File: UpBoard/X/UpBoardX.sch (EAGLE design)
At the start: 120 parts, among them CN1 100nF, CN2 100nF, CN3 100nF, CN4 100nF, IC1 SAM3X8E(ARDUINO), IC2 MEGA16U2-MU, J1 2POSTERMINALBLOCK.25"PITCH, Q1 FDS5680, Q2 FDS5680, Q3 FDS5680, Q4 FDS5680, Q5 SSMJ328R,LF, Q6 2N7002E, Q8 2N7002E, X1 COMS, X2 COMS, X3 GP, X4 CTRL/PYRO, Y1 FH1200001, Y2 ABS05, Y3 406C35D16M00000

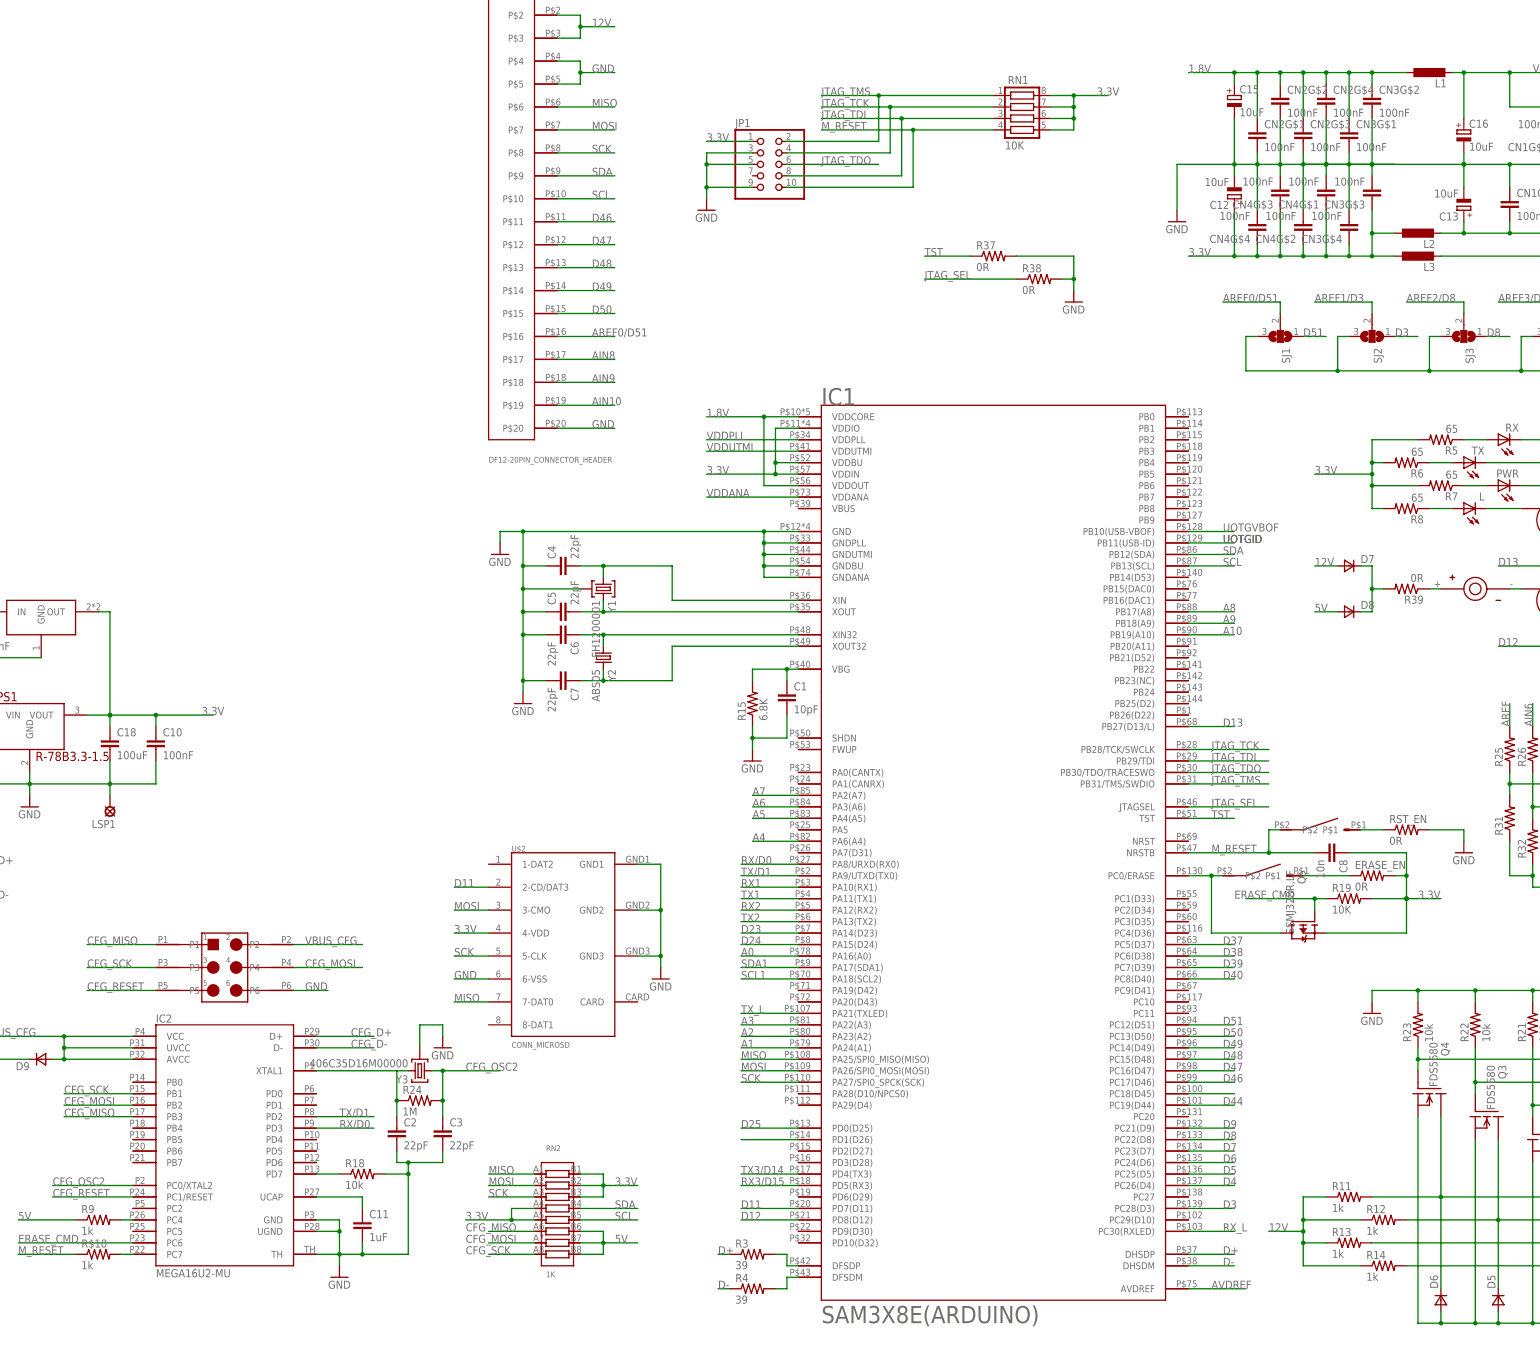
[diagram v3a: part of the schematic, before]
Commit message: Finished labeling, removed SPI pull ups
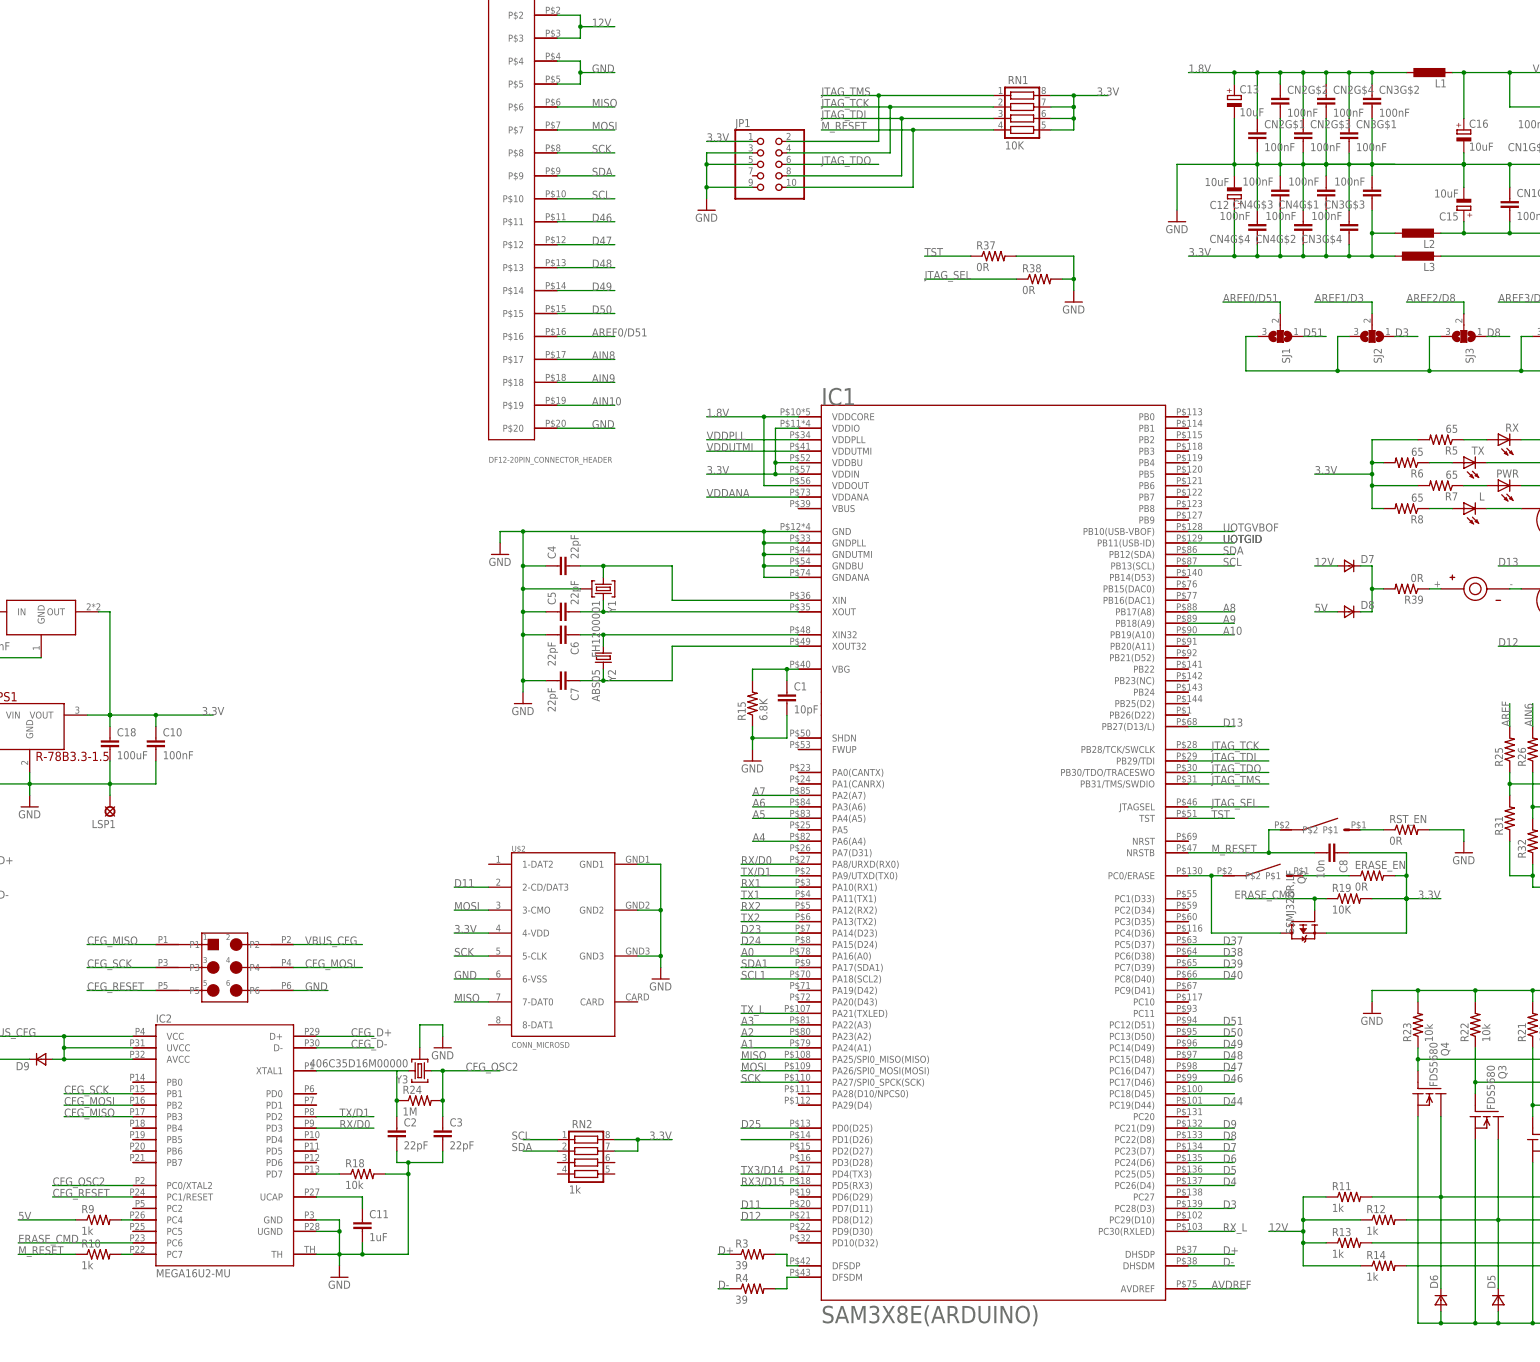
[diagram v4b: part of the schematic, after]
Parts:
- RN2: value 1K -> 1k; device resistor-net:EXB-2HV102JV -> resistor-net:CTS742C083
- renumbered R$10 to R10
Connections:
- net 1.8V: now also C13.+; no longer C15.+
- net 3.3V: now also RN2.7, RN2.8; no longer RN2.A4, RN2.A5, RN2.B1, RN2.B2, RN2.B3
- net 5V: no longer RN2.B6, RN2.B7, RN2.B8
- net CFG_MISO: no longer RN2.A6
- net CFG_MOSI: no longer RN2.A7
- net CFG_SCK: no longer RN2.A8
- net MISO: no longer RN2.A1
- net MOSI: no longer RN2.A2
- net SCK: no longer RN2.A3
- net SCL: now also RN2.1; no longer RN2.B5
- net SDA: now also RN2.2; no longer RN2.B4
- net VDDANA: now also C15.+; no longer C13.+
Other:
- moved on the sheet: C13, C15

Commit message: First fixes, schematic appearance changes
Connected D+ line on native USB port. Added title block and reorganized
schematic to fit on a size C sheet. Revision number is now 1.
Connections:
- net D+: now also US1.D+
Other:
- note added: "1"
- note added: "Assy:"
- note added: "C"
- note added: "C:/Users/Patrick Chizek/Pictures/CPSSLOGO.bmp"
- note added: "Cal Poly Space Systems"
- note added: "Date:"
- note added: "File: UpBoardX.sch"
- note added: "Project Title:"
- note added: "Revision:"
- note added: "Sheet 1 of 2"
- note added: "Sheet Title:"
- note added: "Size:"
- note added: "UBX Full Schematic"
- note added: "UpBoard X"
- note removed: "SENSOR PACKAGE"
- note removed: "UPBOARD X"
- moved on the sheet: C1, C10, C11, C12, C13, C14, C15, C16, C17, C18, C2, C3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

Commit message: Organized power supply into own module
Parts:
- removed C10, C9: 100nF, resistor:C-EUC0603
- removed C17, C18: 100uF, resistor:C-EUC0805
- removed D1: S10M-TP, UpBoard:S10M-TP
- removed D2: (no value), zetex:DSOD323
- removed PS1: R-78B3.3-1.5, UpBoard B:R-78B3.3-1.5
- removed PS2: AZ1117C, UpBoard B:AZ1117C
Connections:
- removed net VIN: D1.+, J1.P$1
- net 12V: no longer D1.-, D2.A
- net 3.3V: no longer C10.1, C18.1, PS1.VOUT, PS2.OUT
- net 5V: no longer C17.1, C9.1, PS2.IN
- net GND: no longer C10.2, C17.2, C18.2, C9.2, PS1.GND, PS2.GND
- net N$7: now also J1.P$1; no longer D2.C, PS1.VIN
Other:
- note added: "A"
- note added: "Sheet 2 of 2"
- note added: "UBX Power Supply"
- moved on the sheet: LSP1, US1

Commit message: Sheet Changes
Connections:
- net N$7 renamed VIN
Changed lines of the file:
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@@
 </segment>
 </net>
-<net name="N$7" class="0">
+<net name="VIN" class="0">
 <segment>
 <pinref part="J1" gate="G$1" pin="P$1"/>
